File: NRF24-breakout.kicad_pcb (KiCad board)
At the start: 2 copper layers, 27.3 x 30.4 mm, 3 parts, among them J1 CONN_01X08, U1 nRF24

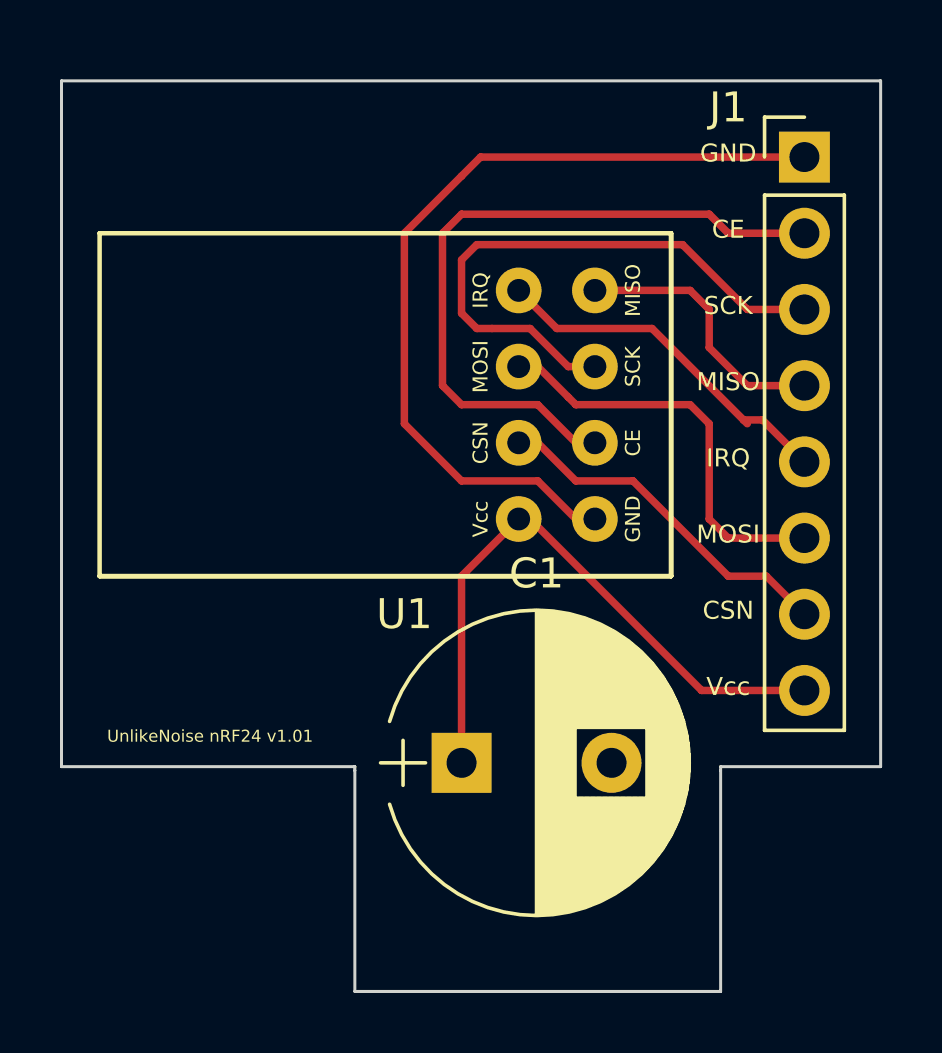
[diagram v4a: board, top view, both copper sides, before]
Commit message: Controlling the track width
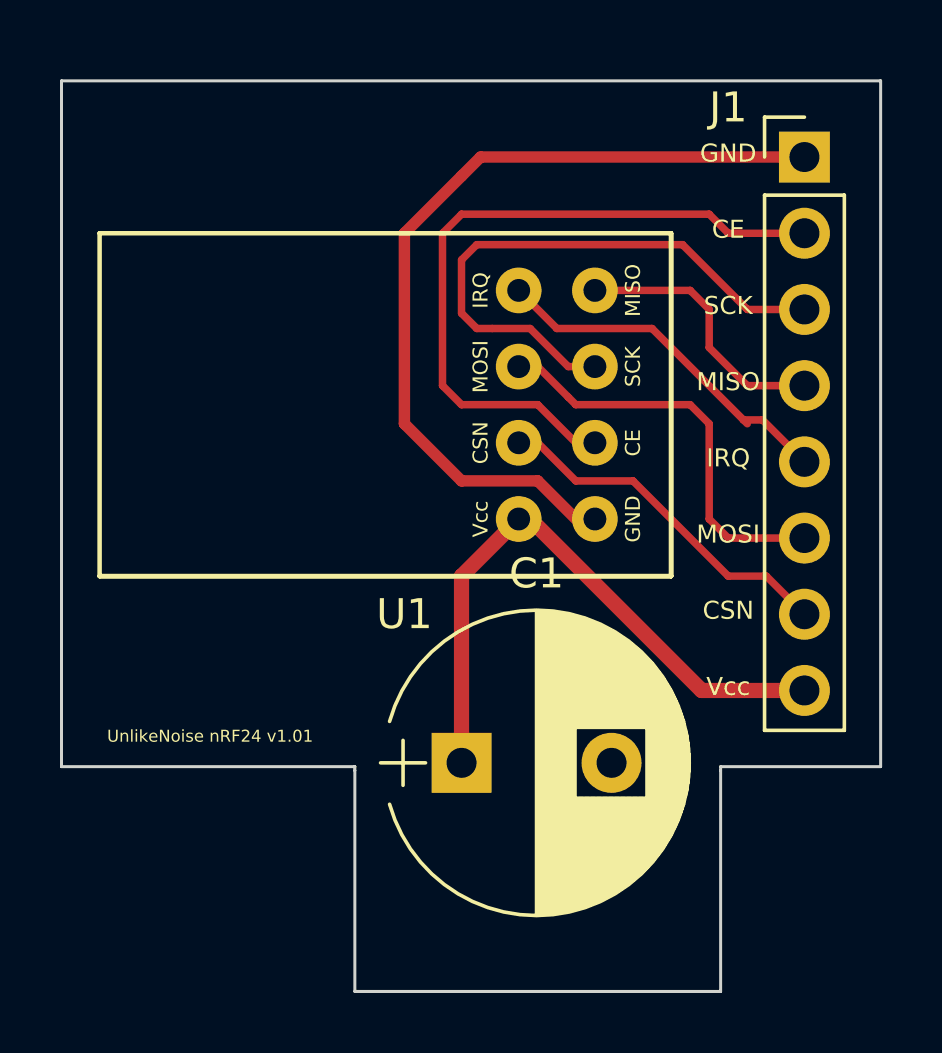
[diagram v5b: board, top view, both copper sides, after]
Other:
- rule trace_min: 0.2 -> 0.1524
- rule via_min_drill: 0.3 -> 0.254
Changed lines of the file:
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@@
     (links 10)
     (no_connects 1)
-    (area 128.854999 114.884999 156.260001 145.338001)
+    (area 128.854999 114.849 158.703334 145.338001)
     (thickness 1.6)
     (drawings 19)
@@
   )
   (setup
-    (last_trace_width 0.25)
+    (last_trace_width 0.381)
+    (user_trace_width 0.1524)
+    (user_trace_width 0.254)
+    (user_trace_width 0.381)
+    (user_trace_width 0.508)
+    (user_trace_width 0.8128)
     (trace_clearance 0.2)
     (zone_clearance 0.508)
     (zone_45_only no)
-    (trace_min 0.2)
+    (trace_min 0.1524)
     (segment_width 0.2)
     (edge_width 0.1)
@@
     (via_drill 0.4)
     (via_min_size 0.4)
-    (via_min_drill 0.3)
+    (via_min_drill 0.254)
+    (user_via 0.4826 0.3302)
+    (user_via 0.5 0.4)
+    (user_via 1.905 0.254)
     (uvia_size 0.3)
     (uvia_drill 0.1)
@@
     (pad_to_mask_clearance 0)
     (aux_axis_origin 0 0)
-    (visible_elements FFFFFF7F)
+    (visible_elements FFFFEF7F)
     (pcbplotparams
       (layerselection 0x00030_80000001)
@@
   (segment (start 152.4 131.445) (end 153.67 132.715) (width 0.25) (layer F.Cu) (net 6))
   (segment (start 144.145 127) (end 144.78 127) (width 0.25) (layer F.Cu) (net 6))
-  (segment (start 142.24 137.668) (end 142.24 131.445) (width 0.25) (layer F.Cu) (net 7))
-  (segment (start 142.24 131.445) (end 144.145 129.54) (width 0.25) (layer F.Cu) (net 7))
-  (segment (start 144.145 129.54) (end 144.526 129.54) (width 0.25) (layer F.Cu) (net 7))
-  (segment (start 144.526 129.54) (end 150.241 135.255) (width 0.25) (layer F.Cu) (net 7))
-  (segment (start 150.241 135.255) (end 153.67 135.255) (width 0.25) (layer F.Cu) (net 7))
+  (segment (start 142.24 137.668) (end 142.24 131.445) (width 0.508) (layer F.Cu) (net 7))
+  (segment (start 142.24 131.445) (end 144.145 129.54) (width 0.508) (layer F.Cu) (net 7))
+  (segment (start 144.145 129.54) (end 144.526 129.54) (width 0.508) (layer F.Cu) (net 7))
+  (segment (start 144.526 129.54) (end 150.241 135.255) (width 0.508) (layer F.Cu) (net 7))
+  (segment (start 150.241 135.255) (end 153.67 135.255) (width 0.508) (layer F.Cu) (net 7))
   (segment (start 146.685 129.54) (end 146.05 129.54) (width 0.25) (layer F.Cu) (net 8))
-  (segment (start 146.05 129.54) (end 144.78 128.27) (width 0.25) (layer F.Cu) (net 8))
-  (segment (start 144.78 128.27) (end 142.24 128.27) (width 0.25) (layer F.Cu) (net 8))
-  (segment (start 142.875 117.475) (end 153.67 117.475) (width 0.25) (layer F.Cu) (net 8))
-  (segment (start 142.24 118.11) (end 142.875 117.475) (width 0.25) (layer F.Cu) (net 8))
-  (segment (start 140.335 120.015) (end 142.24 118.11) (width 0.25) (layer F.Cu) (net 8))
-  (segment (start 140.335 126.365) (end 140.335 120.015) (width 0.25) (layer F.Cu) (net 8))
-  (segment (start 142.24 128.27) (end 140.335 126.365) (width 0.25) (layer F.Cu) (net 8))
+  (segment (start 146.05 129.54) (end 144.78 128.27) (width 0.381) (layer F.Cu) (net 8))
+  (segment (start 144.78 128.27) (end 142.24 128.27) (width 0.381) (layer F.Cu) (net 8))
+  (segment (start 142.875 117.475) (end 153.67 117.475) (width 0.381) (layer F.Cu) (net 8))
+  (segment (start 142.24 118.11) (end 142.875 117.475) (width 0.381) (layer F.Cu) (net 8))
+  (segment (start 140.335 120.015) (end 142.24 118.11) (width 0.381) (layer F.Cu) (net 8))
+  (segment (start 140.335 126.365) (end 140.335 120.015) (width 0.381) (layer F.Cu) (net 8))
+  (segment (start 142.24 128.27) (end 140.335 126.365) (width 0.381) (layer F.Cu) (net 8))
 )

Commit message: Copper GND fills
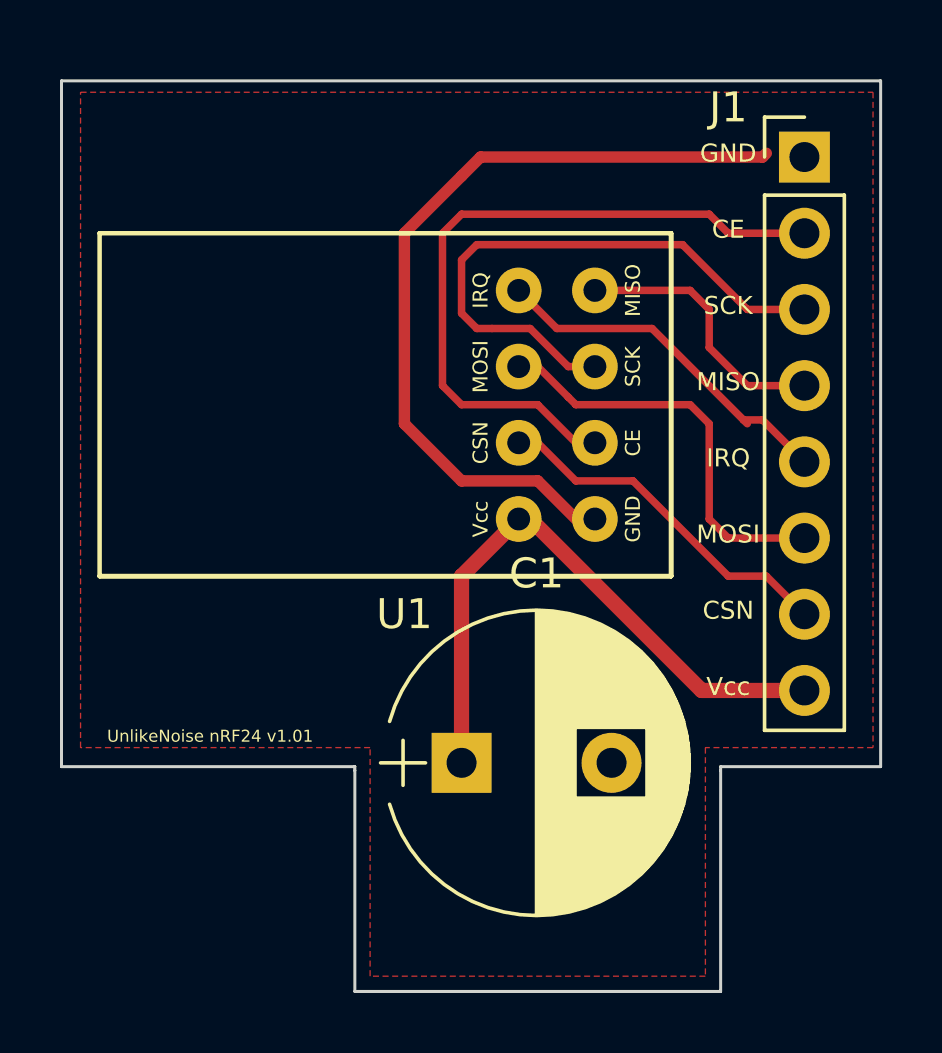
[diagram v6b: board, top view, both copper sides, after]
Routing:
- net Net-(C1-Pad2): track 28.4 -> 26.5 mm
- added copper zone on F.Cu, net Net-(C1-Pad2)
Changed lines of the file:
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@@
   (general
     (links 10)
-    (no_connects 1)
-    (area 128.854999 114.849 158.703334 145.338001)
+    (no_connects 0)
+    (area 128.854999 114.884999 156.260001 145.338001)
     (thickness 1.6)
     (drawings 19)
@@
     (35 F.Paste user)
     (36 B.SilkS user)
-    (37 F.SilkS user)
+    (37 F.SilkS user hide)
     (38 B.Mask user)
     (39 F.Mask user)
@@
     (47 F.CrtYd user)
     (48 B.Fab user)
-    (49 F.Fab user)
+    (49 F.Fab user hide)
   )
   (setup
@@
     (pad_to_mask_clearance 0)
     (aux_axis_origin 0 0)
-    (visible_elements FFFFEF7F)
+    (visible_elements FFFFFF7F)
     (pcbplotparams
       (layerselection 0x00030_80000001)
@@
   (segment (start 144.526 129.54) (end 150.241 135.255) (width 0.508) (layer F.Cu) (net 7))
   (segment (start 150.241 135.255) (end 153.67 135.255) (width 0.508) (layer F.Cu) (net 7))
-  (segment (start 146.685 129.54) (end 146.05 129.54) (width 0.25) (layer F.Cu) (net 8))
+  (segment (start 142.875 117.475) (end 152.273 117.475) (width 0.381) (layer F.Cu) (net 8))
   (segment (start 146.05 129.54) (end 144.78 128.27) (width 0.381) (layer F.Cu) (net 8))
   (segment (start 144.78 128.27) (end 142.24 128.27) (width 0.381) (layer F.Cu) (net 8))
-  (segment (start 142.875 117.475) (end 153.67 117.475) (width 0.381) (layer F.Cu) (net 8))
   (segment (start 142.24 118.11) (end 142.875 117.475) (width 0.381) (layer F.Cu) (net 8))
   (segment (start 140.335 120.015) (end 142.24 118.11) (width 0.381) (layer F.Cu) (net 8))
   (segment (start 140.335 126.365) (end 140.335 120.015) (width 0.381) (layer F.Cu) (net 8))
   (segment (start 142.24 128.27) (end 140.335 126.365) (width 0.381) (layer F.Cu) (net 8))
+  (segment (start 152.273 117.475) (end 152.4 117.348) (width 0.381) (layer F.Cu) (net 8))
+  (zone (net 8) (net_name "Net-(C1-Pad2)") (layer F.Cu) (hatch edge 0.508)
+    (connect_pads (clearance 0.508))
+    (min_thickness 0.254)
+    (fill yes (arc_segments 16) (thermal_gap 0.508) (thermal_bridge_width 0.508))
+    (polygon
+      (pts
+        (xy 155.956 137.16) (xy 150.368 137.16) (xy 150.368 144.78) (xy 139.192 144.78) (xy 139.192 137.16)
+        (xy 129.54 137.16) (xy 129.54 115.316) (xy 155.956 115.316)
+      )
+    )
+  )
 )
